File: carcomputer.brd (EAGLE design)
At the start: 112.7 x 95.9 mm, 76 parts, among them IC1 LM358N, K1 351, K2 RT184012, K3 RT184012, Q1 BS170, Q5 TIP136, T1 BC618, T2 BC618, T3 BC618, T4 BC618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

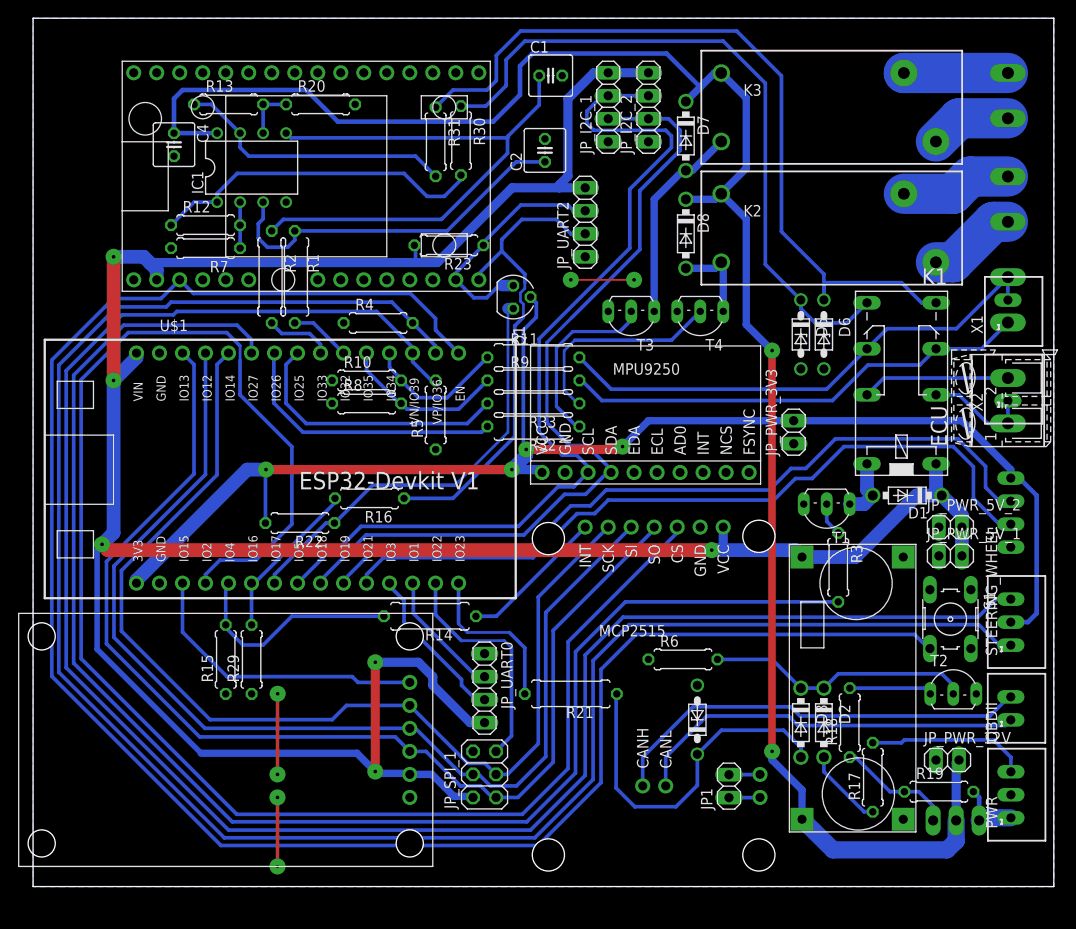
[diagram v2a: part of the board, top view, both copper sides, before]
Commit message: Placed labels next to components. Rearranged silkscreen. Improved vias
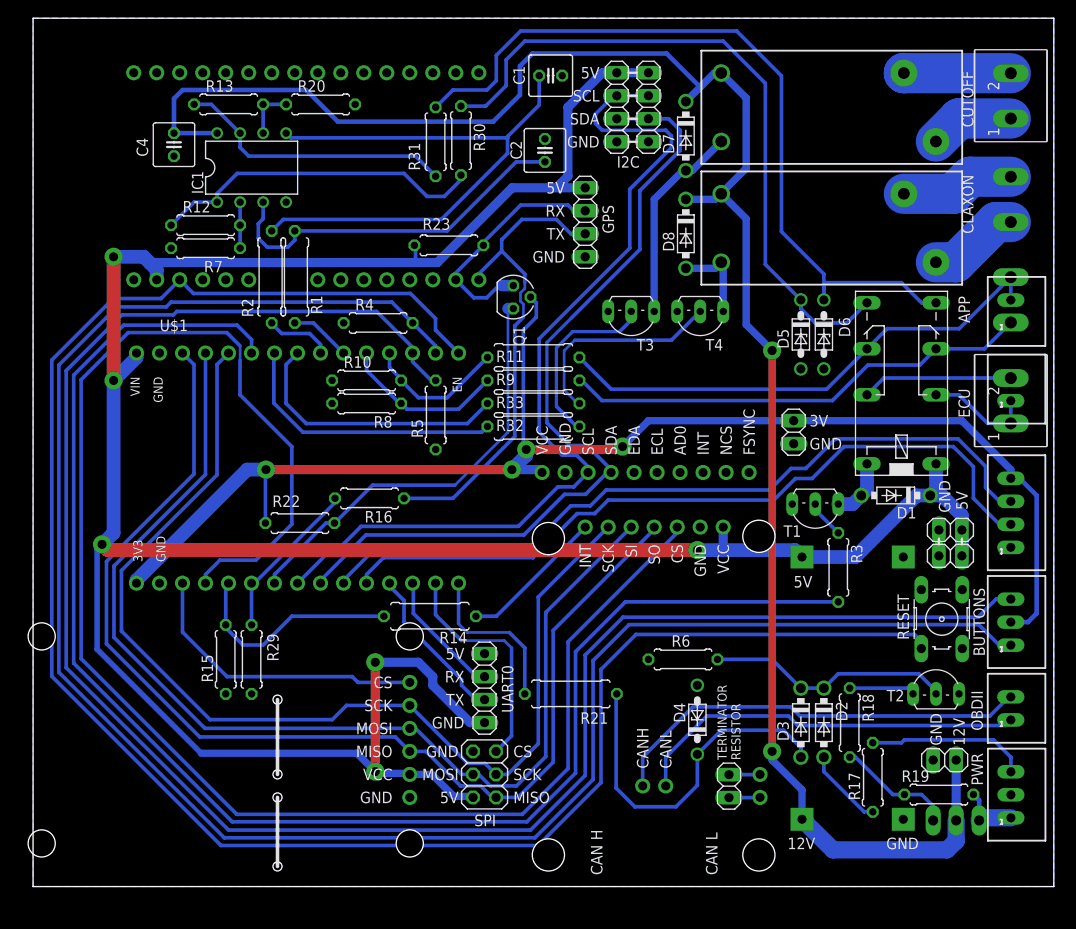
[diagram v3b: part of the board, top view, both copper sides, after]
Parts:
- removed S1: (no value), switch-omron:B3F-10XX
- added RESET: (no value), switch-omron:B3F-10XX
- moved T2 1.91 mm to (88.6, 15.2)
- moved D1 1.27 mm to (84.1, 35.9)
- moved T1 1.27 mm to (75.2, 33.7)
- moved JP_I2C_1 0.95 mm to (53.3, 78.7)
- moved APP 0.32 mm to (96.8, 57.5)
- moved CLAXON_CONN 0.32 mm to (96.8, 68.6), turned to 90 degrees
- moved ECU 0.32 mm to (96.8, 46.4)
- moved ENGINE_CUTOFF_CONN 0.32 mm to (96.8, 80.0), flipped to the top, turned to 90 degrees
- moved JP_PWR_12V 0.32 mm to (89.5, 6.67)
- moved X1 0.32 mm to (96.8, 56.2)
- moved X2 0.32 mm to (96.8, 47.6)
- moved R19 0.32 mm to (88.9, 2.86)
- moved JP_PWR_5V_2 0.32 mm to (90.2, 32.1)
- flipped DISPLAY to the top, turned to 90 degrees
- renumbered JP1 to CAN_TERM_RESISTOR
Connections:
- net +3V3: now also DISPLAY.4; no longer DISPLAY.1
- net GND: now also DISPLAY.1, RESET.1, RESET.2; no longer DISPLAY.4, S1.1, S1.2
- net I2C1_SCL: now also DISPLAY.3; no longer DISPLAY.2
- net I2C1_SDA: now also DISPLAY.2; no longer DISPLAY.3
- net MCU_RESET: now also RESET.3, RESET.4; no longer S1.3, S1.4
- net N$19: now also ENGINE_CUTOFF_CONN.2; no longer ENGINE_CUTOFF_CONN.1
- net N$20: now also ENGINE_CUTOFF_CONN.1; no longer ENGINE_CUTOFF_CONN.2
- net N$27: now also CLAXON_CONN.2; no longer CLAXON_CONN.1
- net N$28: now also CLAXON_CONN.1; no longer CLAXON_CONN.2
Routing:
- net GND: track 23.5 -> 0.00 mm, vias 6 -> 0
- net N$5: track 29.5 -> 27.2 mm
- net I2C0_SCL: track 102.3 -> 100.2 mm
- net N$15: track 9.15 -> 7.25 mm
- net I2C0_SDA: track 93.7 -> 92.8 mm
- net +5V: track 314.1 -> 313.5 mm
- net N$2: track 3.70 -> 4.23 mm
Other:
- board text added: "12V"
- board text added: "3V"
- board text added: "5V"
- board text added: "BUTTONS"
- board text added: "CAN H"
- board text added: "CAN L"
- board text added: "CLAXON"
- board text added: "CS"
- board text added: "CUTOFF"
- board text added: "GND"
- board text added: "GPS"
- board text added: "I2C"
- board text added: "MISO"
- board text added: "MOSI"
- board text added: "RX"
- board text added: "SCK"
- board text added: "SCL"
- board text added: "SDA"
- board text added: "SPI"
- board text added: "TERMINATOR RESISTOR"
- board text added: "TX"
- board text added: "UART0"

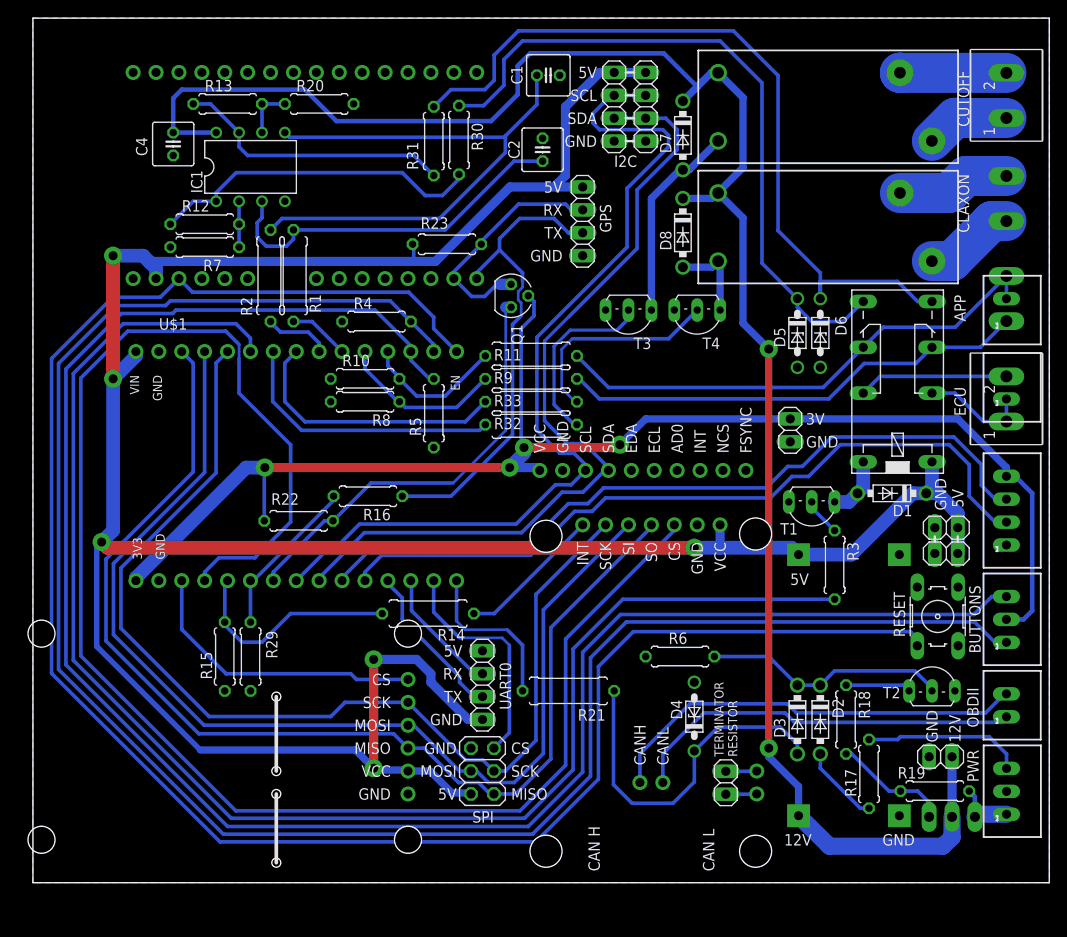
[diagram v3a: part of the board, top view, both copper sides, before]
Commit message: Updated silkscreen
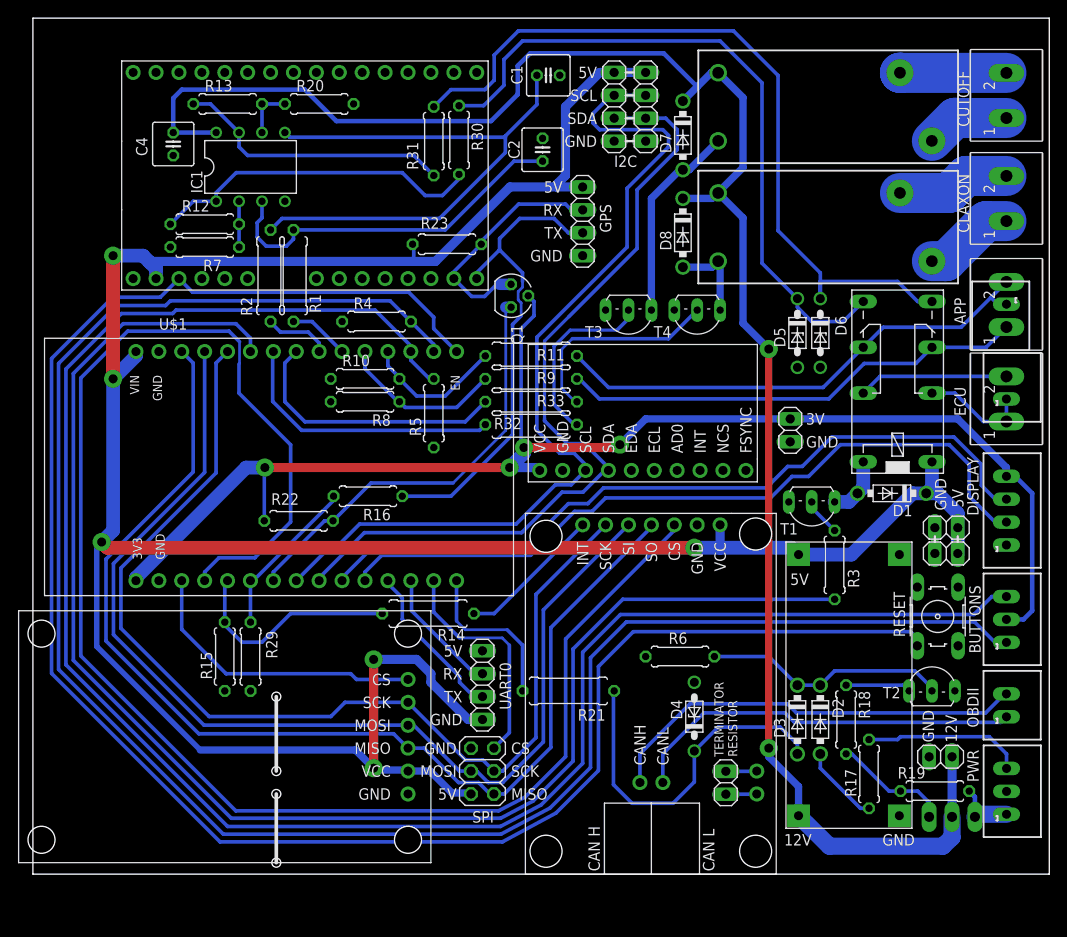
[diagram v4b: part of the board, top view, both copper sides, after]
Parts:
- moved APP 0.63 mm to (96.8, 56.8), flipped to the top, turned to 90 degrees
- moved X1 0.63 mm to (96.8, 55.6), turned to 270 degrees
- flipped CLAXON_CONN to the top
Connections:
- net APP_0_IN: now also APP.2, X1.1; no longer APP.1, X1.2
- net APP_1_IN: now also APP.1, X1.2; no longer APP.2, X1.1
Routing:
- net MCU_RESET: track 209.4 -> 208.3 mm
- net BTN_0: track 212.2 -> 211.2 mm
- net BTN_1: track 210.4 -> 209.5 mm
- net APP_ENABLE: track 165.4 -> 164.6 mm
- net APP_0_IN: track 56.7 -> 56.0 mm
- net SPI_MISO: track 125.2 -> 124.4 mm
- net SPI_MOSI: track 120.6 -> 119.9 mm
- net CAN_CS: track 180.6 -> 180.0 mm
- removed copper zone on layer 16, net GND
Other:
- board size 112.7 x 95.9 mm -> 112.7 x 94.9 mm

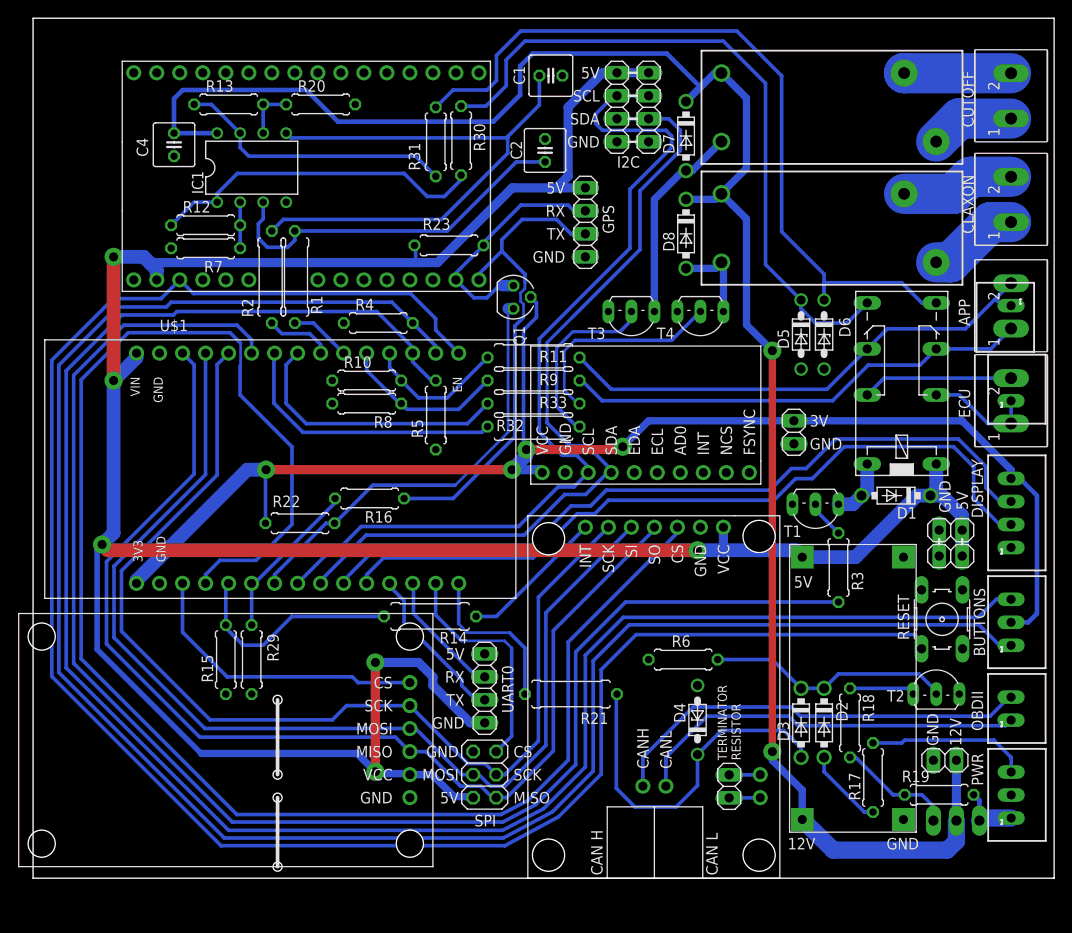
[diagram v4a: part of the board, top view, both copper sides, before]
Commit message: Improved traces. Renamed claxon/engine connections to more common names
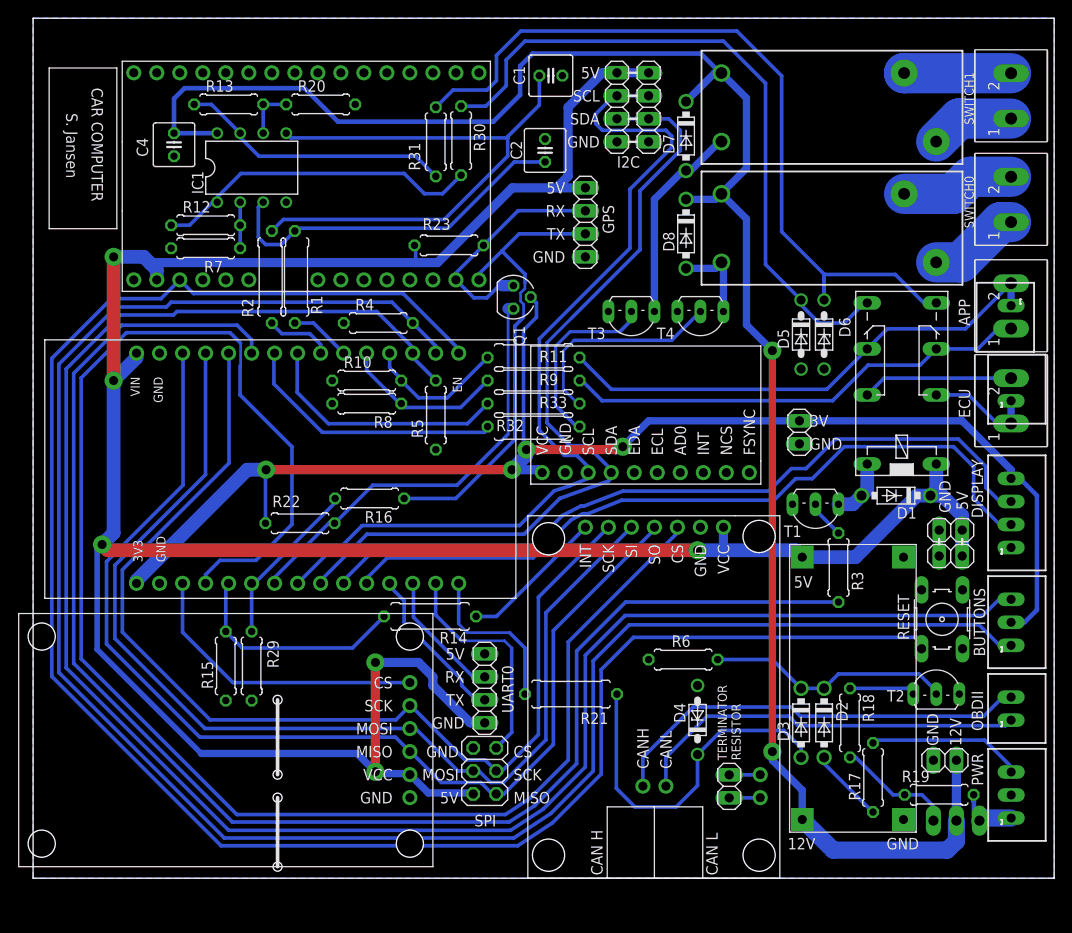
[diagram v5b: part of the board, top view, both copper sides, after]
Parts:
- moved R15 0.71 mm to (10.2, 17.1)
- moved R29 0.71 mm to (13.0, 17.1)
- moved JP_PWR_3V3 0.61 mm to (73.5, 42.9)
- moved JP_SPI_1 0.41 mm to (38.7, 5.49)
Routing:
- net CLAXON_ENABLE: track 30.2 -> 27.7 mm
- net GPS_TX: track 53.6 -> 51.7 mm
- net SPI_MISO: track 124.4 -> 122.6 mm
- net PWR_IN+: track 200.5 -> 202.2 mm
- net N$3: track 87.2 -> 88.5 mm
- net ENGINE_CUTOFF_DISABLE: track 30.7 -> 29.7 mm
- net N$8: track 40.8 -> 39.9 mm
- net N$4: track 37.3 -> 36.5 mm
- net SPI_SCK: track 117.8 -> 117.0 mm
- net SPI_MOSI: track 119.9 -> 119.1 mm
- net UART2_RX: track 18.0 -> 18.7 mm
- net GPS_RX: track 26.4 -> 25.7 mm
- net I2C1_SDA: track 83.5 -> 82.9 mm
- net N$18: track 30.9 -> 30.2 mm
- net IGNITION: track 17.8 -> 17.2 mm
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- added copper zone on layer 16, net GND
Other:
- board text added: "CAR COMPUTER"
- board text added: "S. Jansen"
- board text added: "SWITCH0"
- board text added: "SWITCH1"
- board text removed: "CLAXON"
- board text removed: "CUTOFF"

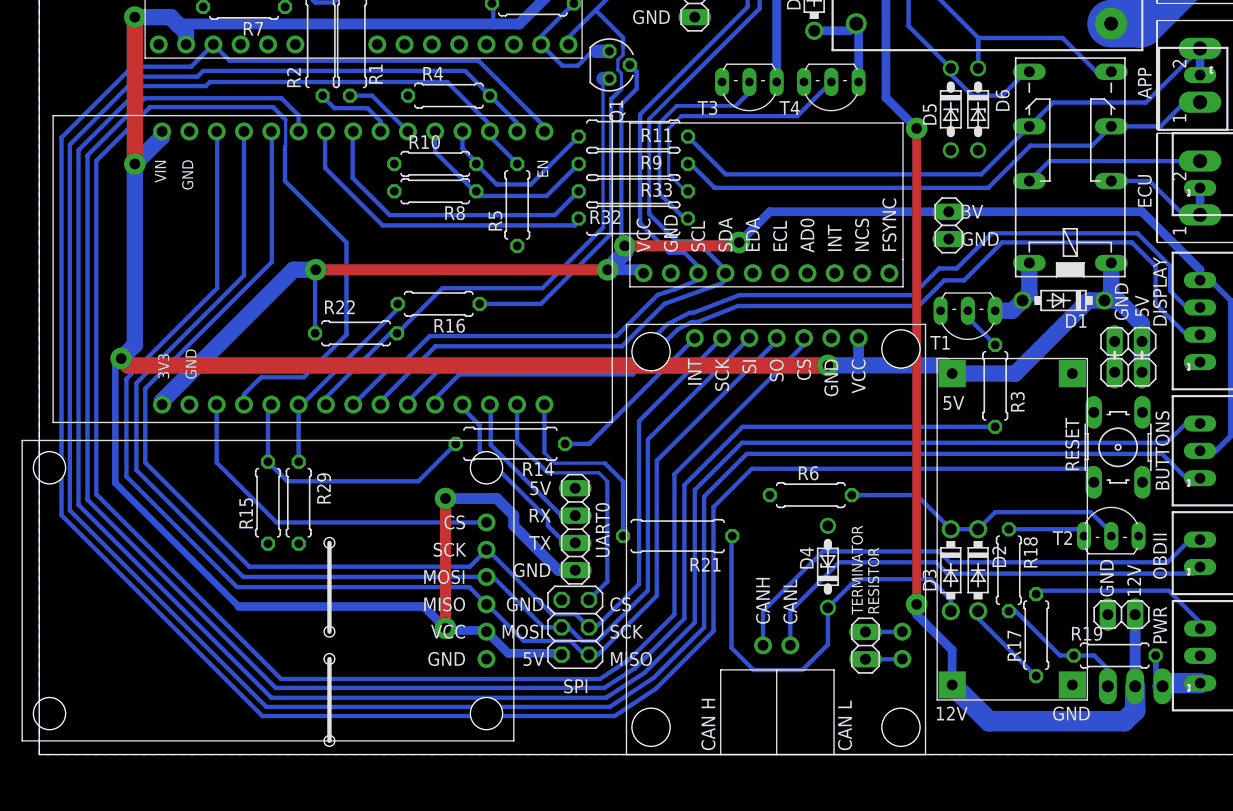
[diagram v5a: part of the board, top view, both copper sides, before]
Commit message: Added volage divider for MISO. Also added more space to some tracks.
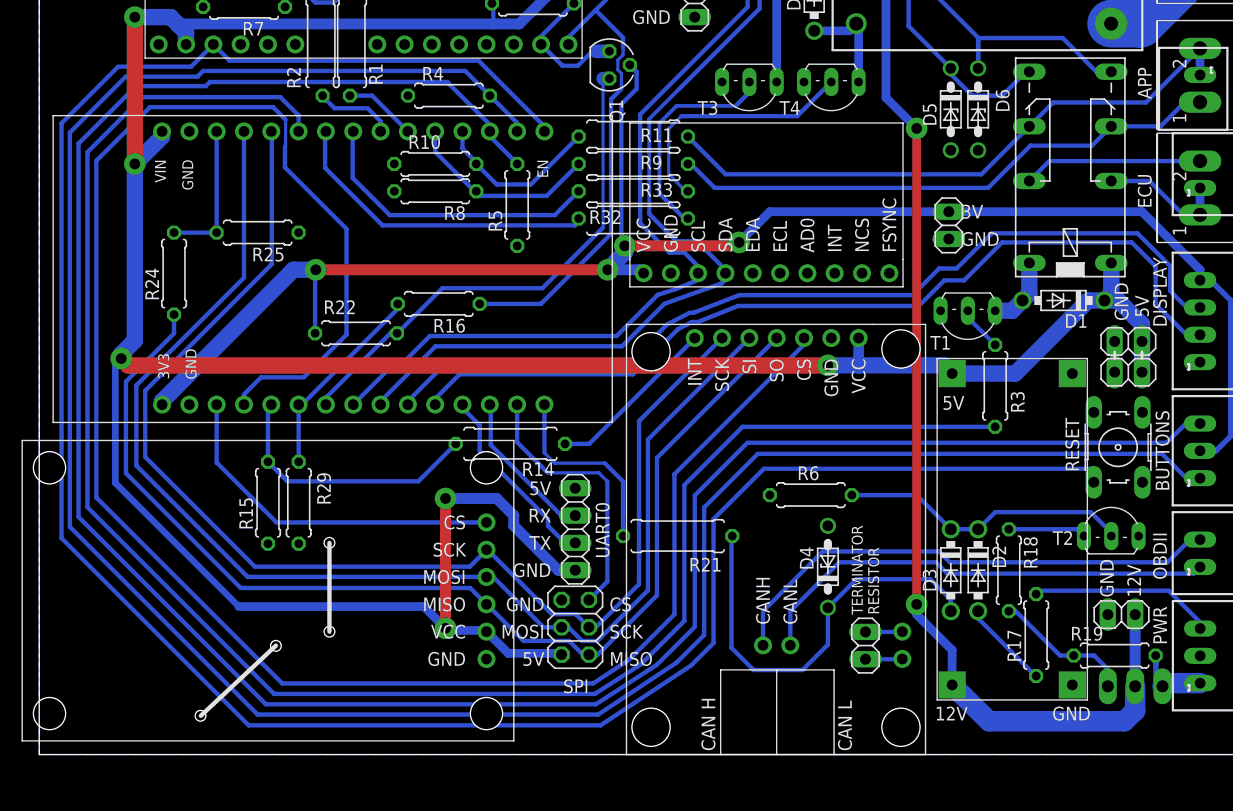
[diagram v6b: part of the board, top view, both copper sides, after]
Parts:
- added R24: 5k, rcl:0207/7
- added R25: 10k, rcl:0207/7
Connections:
- new net SPI_MISO_5V: JP_SPI_1.1, R24.1, U$2.SO, U$5.MISO
- net GND: now also R25.1
- net SPI_MISO: now also R24.2, R25.2; no longer JP_SPI_1.1, U$2.SO, U$5.MISO
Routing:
- net SPI_MISO: track 122.6 -> 13.4 mm
- net SPI_MISO_5V: track 0.00 -> 103.8 mm
- net MCU_RESET: track 208.2 -> 210.6 mm
- net BTN_0: track 211.4 -> 213.2 mm
- net BTN_1: track 209.5 -> 210.7 mm
- net APP_ENABLE: track 164.8 -> 165.9 mm
